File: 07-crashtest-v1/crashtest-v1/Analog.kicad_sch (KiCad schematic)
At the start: 20 parts, among them IC2 AD7175-8BCPZ-RL7, U2 DAC60501ZDGSR

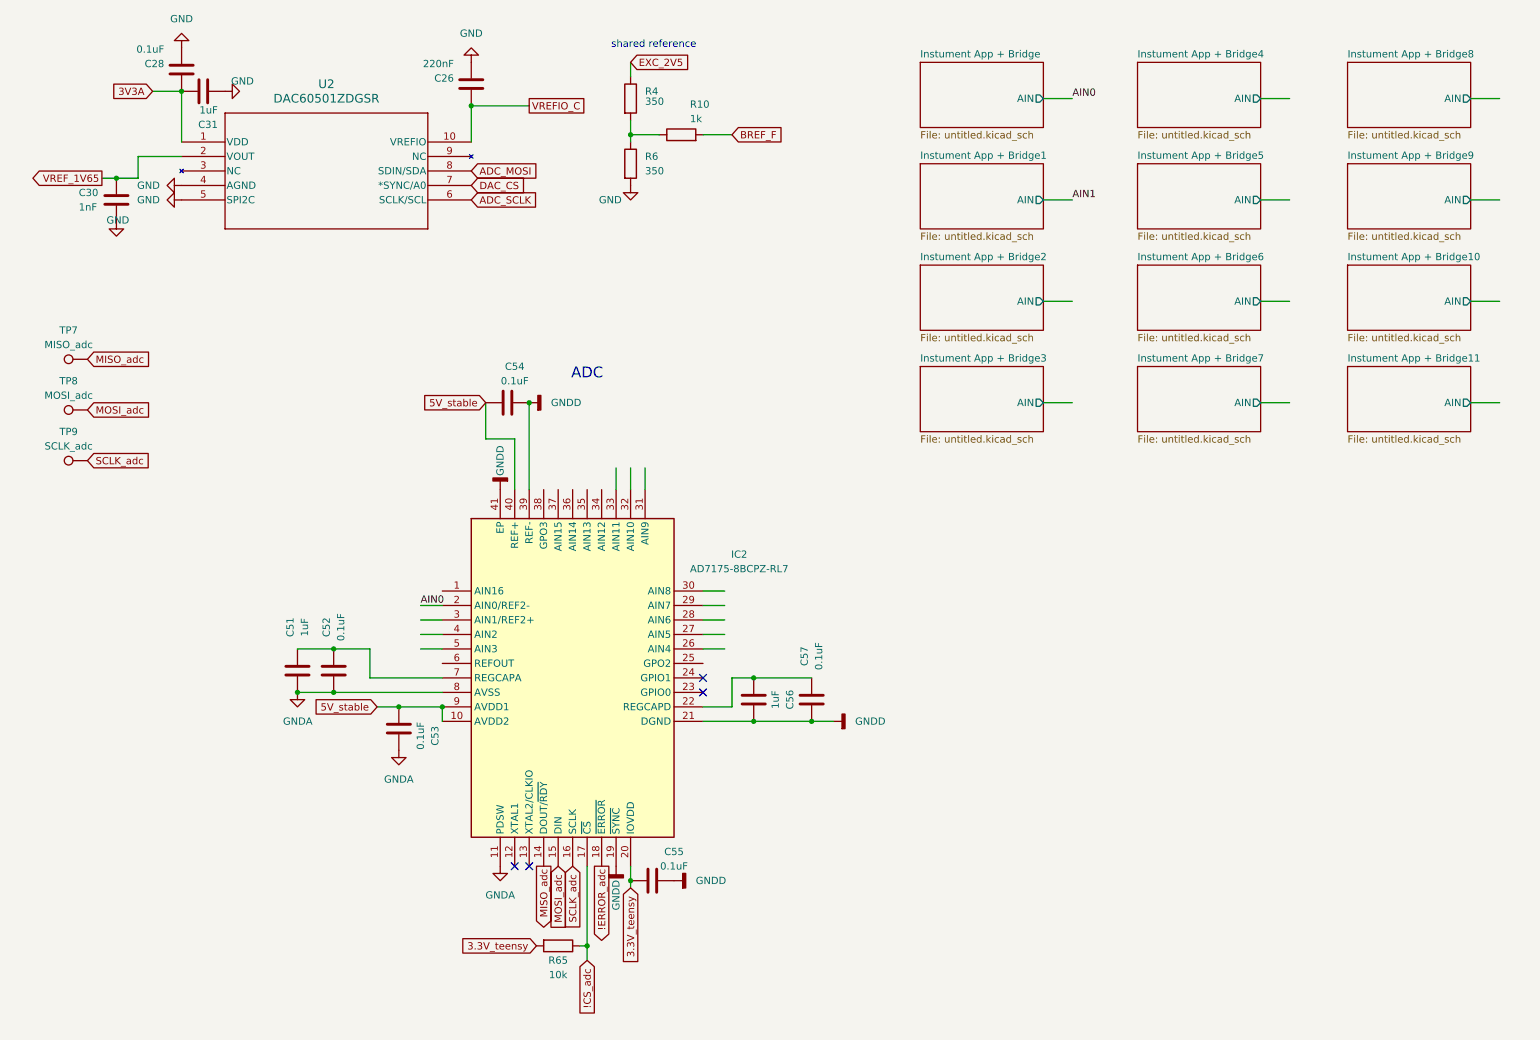
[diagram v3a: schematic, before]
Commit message: mcu pinout started
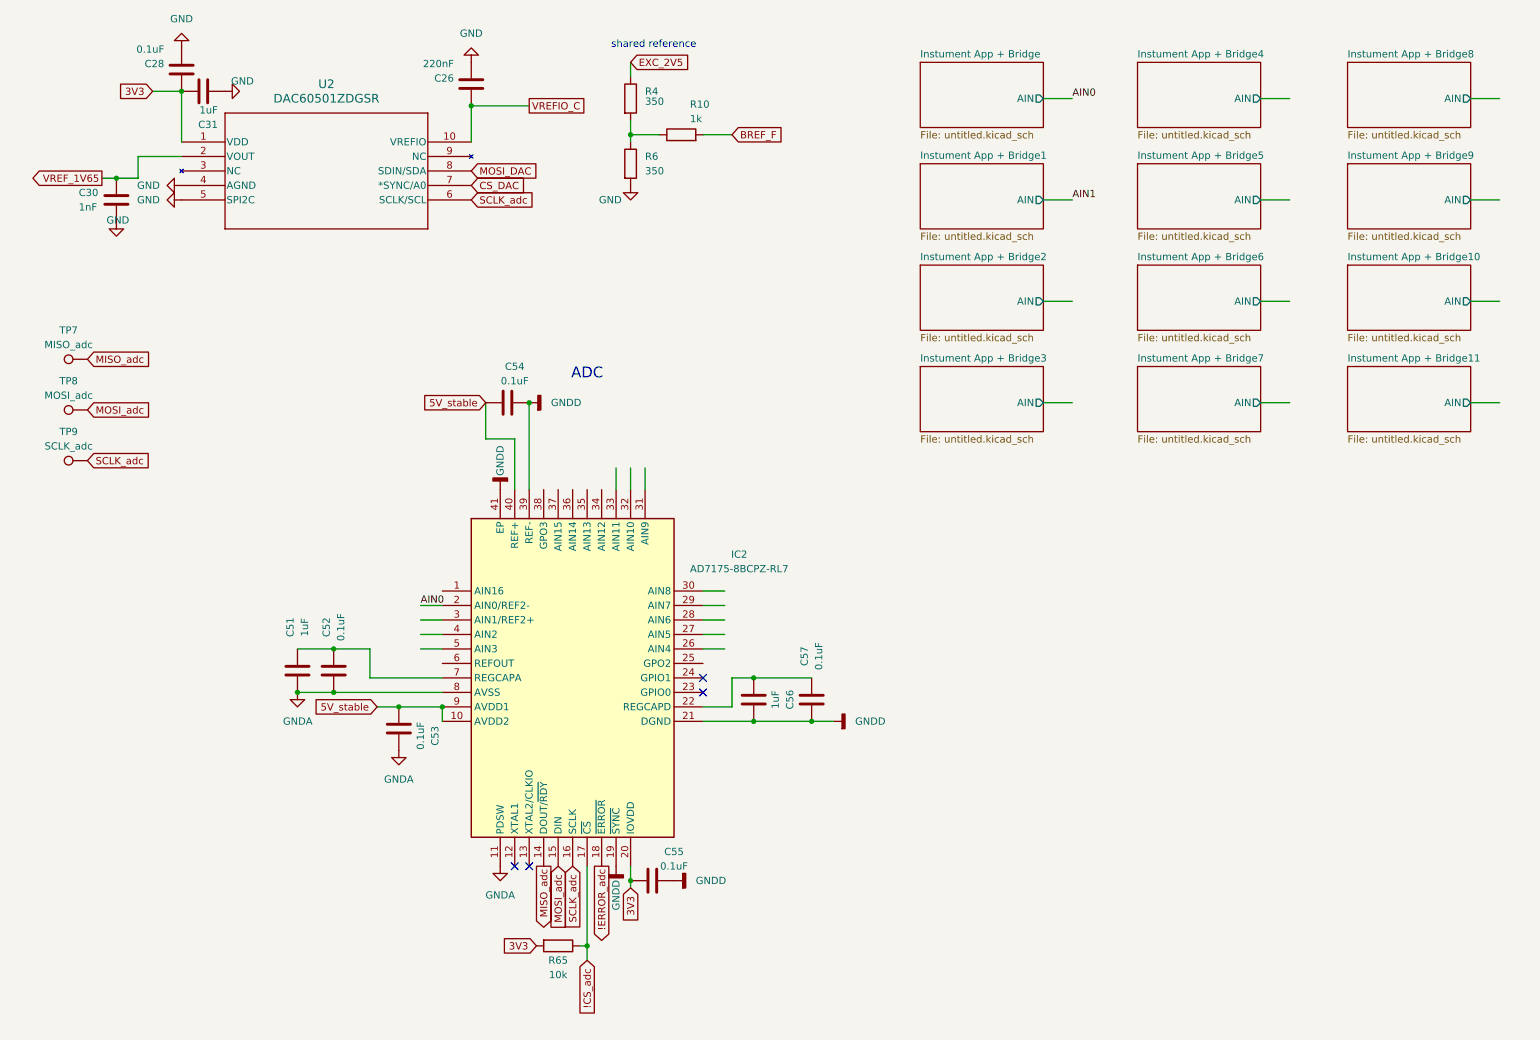
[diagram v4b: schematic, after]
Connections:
- net 3V3A is gone; now on net 3V3: C28.2, C31.2, U2.1 (VDD)
- net ADC_SCLK is gone; now on net SCLK_adc: U2.6 (SCLK/SCL)
- net 3.3V_teensy renamed 3V3
- net ADC_MOSI renamed MOSI_DAC
- net DAC_CS renamed CS_DAC
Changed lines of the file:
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@@
 		)
 	)
-	(global_label "DAC_CS"
-		(shape input)
-		(at 90.17 44.45 0)
-		(fields_autoplaced yes)
-		(effects
-			(font
-				(size 1.27 1.27)
-			)
-			(justify left)
-		)
-		(property "Intersheetrefs" "${INTERSHEET_REFS}"
-			(at 100.2309 44.45 0)
+	(global_label "MOSI_DAC"
+		(shape input)
+		(at 90.17 41.91 0)
+		(fields_autoplaced yes)
+		(effects
+			(font
+				(size 1.27 1.27)
+			)
+			(justify left)
+		)
+		(property "Intersheetrefs" "${INTERSHEET_REFS}"
+			(at 101.6934 41.91 0)
 			(hide yes)
 			(show_name no)
@@
 		)
 	)
-	(global_label "ADC_SCLK"
-		(shape input)
-		(at 90.17 46.99 0)
-		(fields_autoplaced yes)
-		(effects
-			(font
-				(size 1.27 1.27)
-			)
-			(justify left)
-		)
-		(property "Intersheetrefs" "${INTERSHEET_REFS}"
-			(at 102.529 46.99 0)
-			(hide yes)
-			(show_name no)
-			(do_not_autoplace no)
-			(effects
-				(font
-					(size 1.27 1.27)
-				)
-				(justify left)
+	(global_label "3V3"
+		(shape input)
+		(at 101.6 177.8 180)
+		(fields_autoplaced yes)
+		(effects
+			(font
+				(size 1.27 1.27)
+			)
+			(justify right)
+		)
+		(property "Intersheetrefs" "${INTERSHEET_REFS}"
+			(at 95.7614 177.8 0)
+			(hide yes)
+			(show_name no)
+			(do_not_autoplace no)
+			(effects
+				(font
+					(size 1.27 1.27)
+				)
+				(justify right)
+			)
+		)
+	)
+	(global_label "3V3"
+		(shape input)
+		(at 118.11 167.64 270)
+		(fields_autoplaced yes)
+		(effects
+			(font
+				(size 1.27 1.27)
+			)
+			(justify right)
+		)
+		(property "Intersheetrefs" "${INTERSHEET_REFS}"
+			(at 118.11 173.4786 90)
+			(hide yes)
+			(show_name no)
+			(do_not_autoplace no)
+			(effects
+				(font
+					(size 1.27 1.27)
+				)
+				(justify right)
 			)
 		)
@@
 		)
 	)
-	(global_label "ADC_MOSI"
-		(shape input)
-		(at 90.17 41.91 0)
-		(fields_autoplaced yes)
-		(effects
-			(font
-				(size 1.27 1.27)
-			)
-			(justify left)
-		)
-		(property "Intersheetrefs" "${INTERSHEET_REFS}"
-			(at 102.3476 41.91 0)
+	(global_label "SCLK_adc"
+		(shape input)
+		(at 90.17 46.99 0)
+		(fields_autoplaced yes)
+		(effects
+			(font
+				(size 1.27 1.27)
+			)
+			(justify left)
+		)
+		(property "Intersheetrefs" "${INTERSHEET_REFS}"
+			(at 101.6328 46.99 0)
+			(hide yes)
+			(show_name no)
+			(do_not_autoplace no)
+			(effects
+				(font
+					(size 1.27 1.27)
+				)
+				(justify left)
+			)
+		)
+	)
+	(global_label "CS_DAC"
+		(shape input)
+		(at 90.17 44.45 0)
+		(fields_autoplaced yes)
+		(effects
+			(font
+				(size 1.27 1.27)
+			)
+			(justify left)
+		)
+		(property "Intersheetrefs" "${INTERSHEET_REFS}"
+			(at 99.5767 44.45 0)
 			(hide yes)
 			(show_name no)
@@
 		)
 	)
-	(global_label "3.3V_teensy"
-		(shape input)
-		(at 118.11 167.64 270)
-		(fields_autoplaced yes)
-		(effects
-			(font
-				(size 1.27 1.27)
-			)
-			(justify right)
-		)
-		(property "Intersheetrefs" "${INTERSHEET_REFS}"
-			(at 118.11 181.7528 90)
-			(hide yes)
-			(show_name no)
-			(do_not_autoplace no)
-			(effects
-				(font
-					(size 1.27 1.27)
-				)
-				(justify right)
-			)
-		)
-	)
-	(global_label "3.3V_teensy"
-		(shape input)
-		(at 101.6 177.8 180)
-		(fields_autoplaced yes)
-		(effects
-			(font
-				(size 1.27 1.27)
-			)
-			(justify right)
-		)
-		(property "Intersheetrefs" "${INTERSHEET_REFS}"
-			(at 87.4872 177.8 0)
-			(hide yes)
-			(show_name no)
-			(do_not_autoplace no)
-			(effects
-				(font
-					(size 1.27 1.27)
-				)
-				(justify right)
-			)
-		)
-	)
-	(global_label "3V3A"
+	(global_label "3V3"
 		(shape input)
 		(at 34.29 27.94 180)
@@
 		)
 		(property "Intersheetrefs" "${INTERSHEET_REFS}"
-			(at 26.7086 27.94 0)
-			(hide yes)
-			(show_name no)
+			(at 28.4514 27.94 0)
+			(hide yes)
+			(show_name no)
